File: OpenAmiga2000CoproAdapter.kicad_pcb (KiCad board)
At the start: 2 copper layers, 111.6 x 37.5 mm, 19 parts, among them CN1 A2000_COPRO_SLOT, P1 CONN_2, P10 CONN_1, P11 CONN_1, P12 CONN_1, P13 CONN_1, P14 CONN_1, P15 CONN_1, P16 CONN_1, P17 CONN_2, P2 CONN_2, P3 CONN_2, P4 CONN_2, P5 CONN_2, P6 OSHW_LOGO, P7 CONN_1, P8 CONN_1, P9 CONN_1, U1 68000D

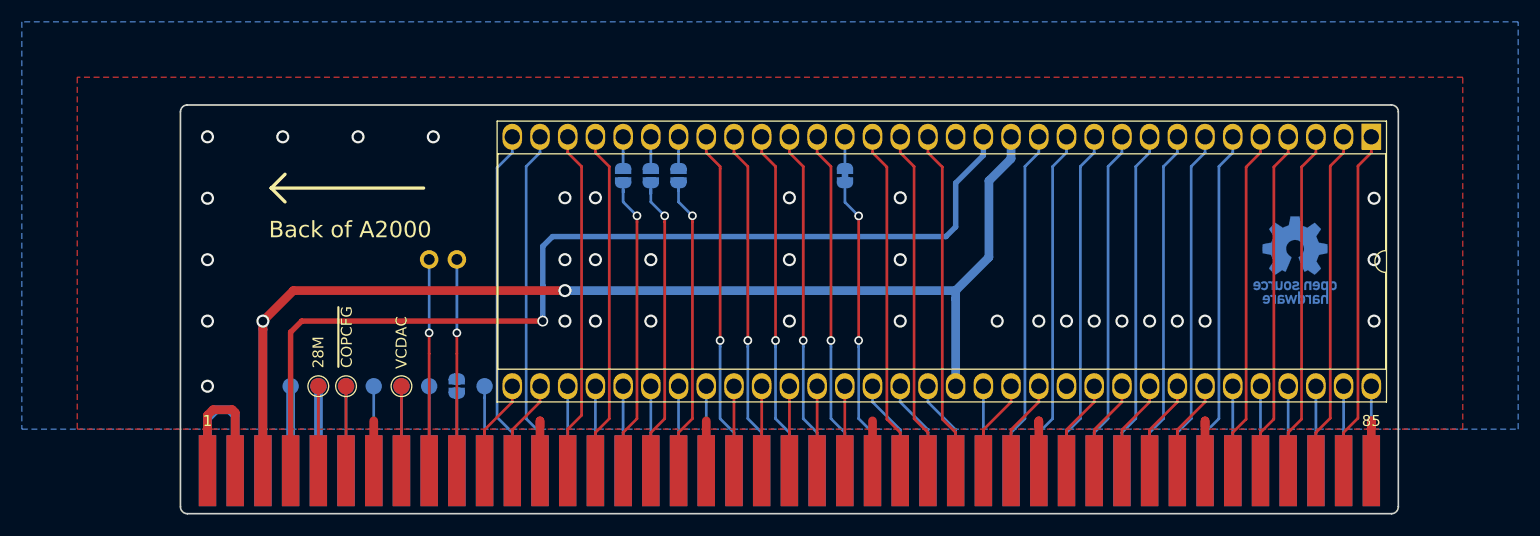
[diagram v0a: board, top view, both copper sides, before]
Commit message: Add CPLD to test out boss functionality
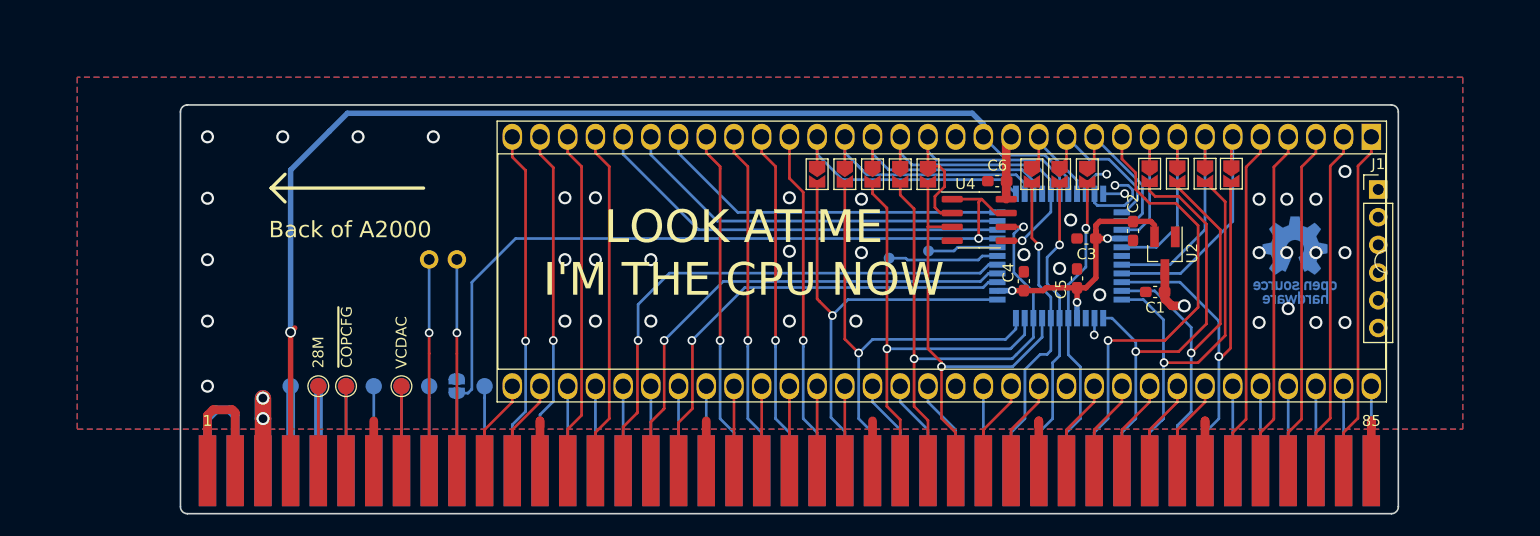
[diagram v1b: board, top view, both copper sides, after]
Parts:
- removed P1: CONN_2, Jumper:SolderJumper-2_P1.3mm_Bridged_RoundedPad1.0x1.5mm
- removed P2, P3, P4: CONN_2, Jumper:SolderJumper-2_P1.3mm_Open_RoundedPad1.0x1.5mm
- added C1: C, Capacitor_SMD:C_0603_1608Metric_Pad1.08x0.95mm_HandSolder, F.Cu at (180.1, 126.4)
- added C2: C, Capacitor_SMD:C_0603_1608Metric_Pad1.08x0.95mm_HandSolder, F.Cu at (178.1, 120.8)
- added C3: C, Capacitor_SMD:C_0603_1608Metric_Pad1.08x0.95mm_HandSolder, F.Cu at (173.8, 121.5)
- added C4: C, Capacitor_SMD:C_0603_1608Metric_Pad1.08x0.95mm_HandSolder, F.Cu at (168.0, 125.4)
- added C5: C, Capacitor_SMD:C_0603_1608Metric_Pad1.08x0.95mm_HandSolder, F.Cu at (172.9, 125.1)
- added C6: C, Capacitor_SMD:C_0603_1608Metric_Pad1.08x0.95mm_HandSolder, F.Cu at (165.6, 116.2)
- added J1: Conn_01x06_Male, Connector_PinHeader_2.54mm:PinHeader_1x06_P2.54mm_Vertical, F.Cu at (200.5, 117.0)
- added JP1: SolderJumper_2_Open, Jumper:SolderJumper-2_P1.3mm_Open_TrianglePad1.0x1.5mm, F.Cu at (156.7, 115.6)
- added JP10: SolderJumper_2_Open, Jumper:SolderJumper-2_P1.3mm_Open_TrianglePad1.0x1.5mm, F.Cu at (171.3, 115.6)
- added JP11: SolderJumper_2_Open, Jumper:SolderJumper-2_P1.3mm_Open_TrianglePad1.0x1.5mm, F.Cu at (154.2, 115.6)
- added JP12: SolderJumper_2_Open, Jumper:SolderJumper-2_P1.3mm_Open_TrianglePad1.0x1.5mm, F.Cu at (149.1, 115.6)
- added JP2: SolderJumper_2_Open, Jumper:SolderJumper-2_P1.3mm_Open_TrianglePad1.0x1.5mm, F.Cu at (159.3, 115.6)
- added JP3: SolderJumper_2_Open, Jumper:SolderJumper-2_P1.3mm_Open_TrianglePad1.0x1.5mm, F.Cu at (151.6, 115.6)
- added JP4: SolderJumper_2_Open, Jumper:SolderJumper-2_P1.3mm_Open_TrianglePad1.0x1.5mm, F.Cu at (168.8, 115.6)
- added JP5: SolderJumper_2_Open, Jumper:SolderJumper-2_P1.3mm_Open_TrianglePad1.0x1.5mm, F.Cu at (173.9, 115.6)
- added JP6: SolderJumper_2_Open, Jumper:SolderJumper-2_P1.3mm_Open_TrianglePad1.0x1.5mm, F.Cu at (179.6, 115.5)
- added JP7: SolderJumper_2_Open, Jumper:SolderJumper-2_P1.3mm_Open_TrianglePad1.0x1.5mm, F.Cu at (182.1, 115.5)
- added JP8: SolderJumper_2_Open, Jumper:SolderJumper-2_P1.3mm_Open_TrianglePad1.0x1.5mm, F.Cu at (184.7, 115.5)
- added JP9: SolderJumper_2_Open, Jumper:SolderJumper-2_P1.3mm_Open_TrianglePad1.0x1.5mm, F.Cu at (187.1, 115.5)
- added TP1: TestPoint, TestPoint:TestPoint_Pad_D1.0mm, B.Cu at (155.7, 123.3)
- added TP2: TestPoint, TestPoint:TestPoint_Pad_D1.0mm, B.Cu at (159.3, 122.6)
- added U2: AP2210N-3.3, Package_TO_SOT_SMD:SOT-23_Handsoldering, F.Cu at (181.0, 122.8)
- added U3: XC9572VQ44, Package_QFP:TQFP-44_10x10mm_P0.8mm, B.Cu at (171.3, 123.1)
- added U4: 74CBTD3306, Package_SO:SOIC-8_3.9x4.9mm_P1.27mm, F.Cu at (164.0, 119.8)
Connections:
- net Net-(CN1-Pad20) renamed /~BOSS
- CN1 pad 31: /fc0 -> /a_FC0
- CN1 pad 33: /fc1 -> /a_FC1
- CN1 pad 35: /fc2 -> /a_FC2
- CN1 pad 50: /e -> /a_E
- CN1 pad 51: /~vma -> /~a_vma
- CN1 pad 53: /~rst -> /~a_rst
- CN1 pad 55: /~hlt -> /~a_hlt
- CN1 pad 60: /~cbr -> /~a_br
- CN1 pad 62: /~bgack -> /~a_bgack
- CN1 pad 64: /~cbg -> /~a_bg
- CN1 pad 68: /r_~w -> /a_r_~w
- CN1 pad 70: /~lds -> /~a_lds
- CN1 pad 72: /~uds -> /~a_uds
- CN1 pad 74: /~as -> /~a_as
- U1 pad 11: /~cbg -> /~c_bg
- U1 pad 12: /~bgack -> /~c_bgack
- U1 pad 13: /~cbr -> /~c_br
- U1 pad 17: /~hlt -> /~c_hlt
- U1 pad 18: /~rst -> /~c_rst
- U1 pad 19: /~vma -> /~c_vma
- U1 pad 20: Net-(P1-Pad2) -> /c_E
- U1 pad 21: /~vpa -> /~c_vpa
- U1 pad 26: Net-(P2-Pad2) -> /c_FC2
- U1 pad 27: Net-(P3-Pad2) -> /c_FC1
- U1 pad 28: Net-(P4-Pad2) -> /c_FC0
- U1 pad 6: /~as -> /~c_as
- U1 pad 7: /~uds -> /~c_uds
- U1 pad 8: /~lds -> /~c_lds
- U1 pad 9: /r_~w -> /c_r_~w
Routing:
- net +5V: track 117.1 -> 24.0 mm, vias 2 -> 3
- net /~BOSS: track 6.69 -> 77.1 mm, vias 0 -> 1
- net +3V3: track 0.00 -> 54.1 mm, vias 0 -> 3
- net /~a_rst: track 0.00 -> 52.2 mm, vias 0 -> 2
- net /a_FC0: track 0.00 -> 50.3 mm, vias 0 -> 1
- net /a_FC1: track 0.00 -> 45.5 mm, vias 0 -> 1
- net /a_E: track 0.00 -> 43.8 mm, vias 0 -> 1
- net /a_FC2: track 0.00 -> 42.7 mm, vias 0 -> 1
- net /~a_vma: track 0.00 -> 42.2 mm, vias 0 -> 1
- net /~a_hlt: track 0.00 -> 42.2 mm, vias 0 -> 1
- net /~a_lds: track 0.00 -> 41.7 mm, vias 0 -> 1
- net /~a_as: track 0.00 -> 41.3 mm, vias 0 -> 1
- net /a_r_~w: track 0.00 -> 40.4 mm, vias 0 -> 1
- net /~a_uds: track 0.00 -> 39.9 mm, vias 0 -> 1
- net /c_FC0: track 0.00 -> 38.8 mm
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- added copper zone on In1.Cu, net +5V
- added copper zone on In2.Cu, net GND
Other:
- copper layers 2 -> 4
- net class Clock removed
- net class Default removed
- net class Power removed
- board text added: "+3.3"
- board text added: "BOSS PROTO"
- board text added: "Bus arbitration copro by LIV2"
- board text added: "LOOK AT ME I'M THE CPU NOW"
- board text added: "TCK"
- board text added: "TDI"
- board text added: "TDO"
- board text added: "TMS"
- board text added: "~BGA"
- board text removed: "V3"
- board text removed: "~BGACK"

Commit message: Boss proto stuff
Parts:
- J1: moved to B.Cu
- turned J1 to 180 degrees
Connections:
- JP7 pad 2: /~a_uds -> /~a_lds
- JP8 pad 2: /~a_lds -> /~a_uds
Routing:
- net GND: track 60.3 -> 53.1 mm, vias 38 -> 42
- net /~a_uds: track 39.9 -> 42.1 mm
- net /a12: track 7.75 -> 8.97 mm
- net Net-(CN1-Pad14): track 7.75 -> 8.88 mm
- net /~a_lds: track 41.7 -> 40.7 mm
- net /d5: track 7.75 -> 8.59 mm
- net /a6: track 8.80 -> 9.45 mm
- net /a23: track 8.80 -> 9.41 mm
- net /a_E: track 43.8 -> 43.2 mm
- added copper zone on In2.Cu, net +5V
- added copper zone on In1.Cu, net GND
- removed copper zone on In1.Cu, net +5V
- removed copper zone on In2.Cu, net GND
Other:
- board text added: "A SECRET MESSAGE"
- board text removed: "LOOK AT ME I'M THE CPU NOW"
